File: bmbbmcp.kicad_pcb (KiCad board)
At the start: 2 copper layers, 57 x 14 mm, 20 parts, among them J1 USB_OTG, J2 Conn_ARM_SWD_TagConnect_TC2030, J3 Conn_01x04_Socket, U1 MDBT50Q-1MV2, U2 AP2112K-3.3, Y1 32.768

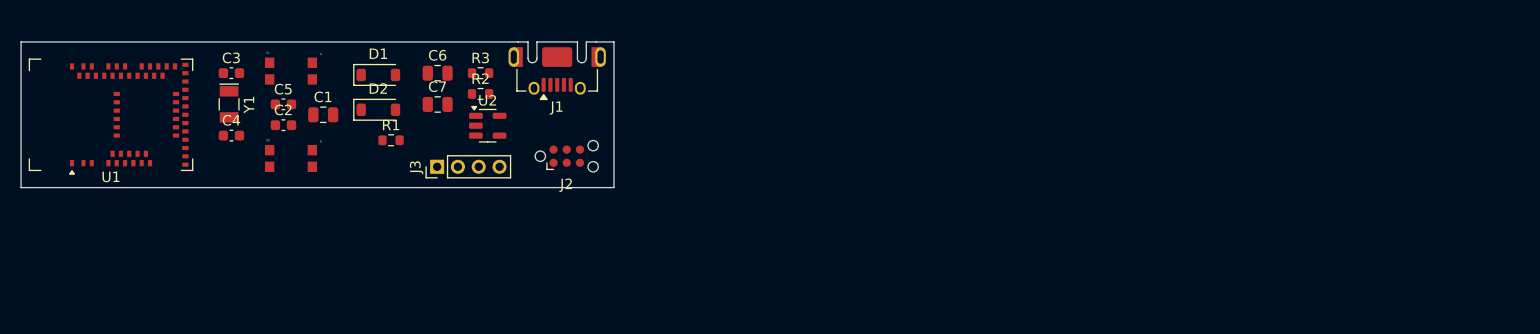
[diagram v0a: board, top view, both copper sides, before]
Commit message: Updated with routing, passes almost all design rule checks
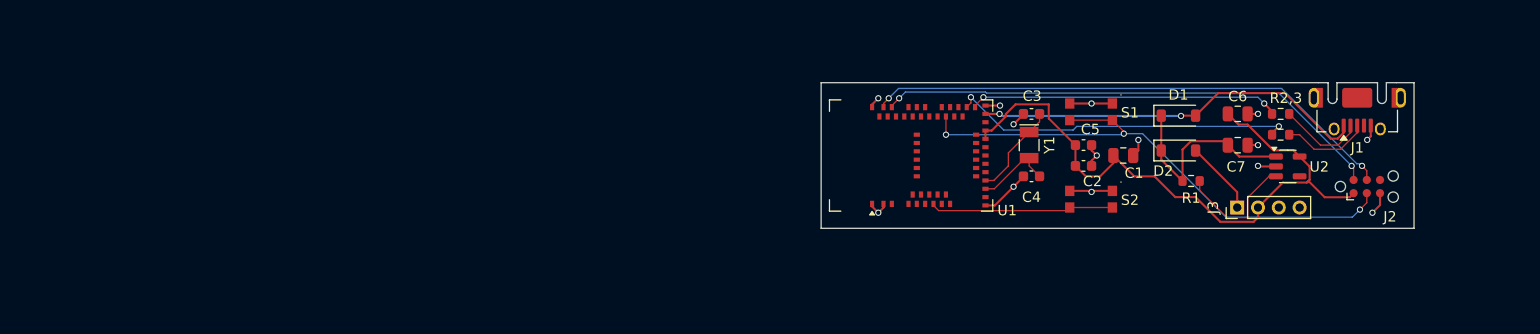
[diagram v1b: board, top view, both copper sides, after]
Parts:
- J2: value Conn_ARM_SWD_TagConnect_TC2030 -> ARM_SWD
- U2: value AP2112K-3.3 -> AP2112K
- moved R1 77.0 mm to (155.5, 95.4)
- moved C1 77.0 mm to (149.0, 92.9)
- moved C6 77.0 mm to (160.0, 88.9)
- moved C7 77.0 mm to (160.0, 91.9)
- moved J1 77.0 mm to (171.5, 87.0)
- moved R2 77.0 mm to (164.1, 90.9)
- moved R2,3 77.0 mm to (164.1, 88.9)
- moved S1 77.0 mm to (145.9, 88.7)
- moved S2 77.0 mm to (145.9, 97.1)
- moved U2 77.0 mm to (164.8, 94.0)
- moved C2 77.0 mm to (145.1, 93.9)
- moved C3 77.0 mm to (140.1, 88.9)
- moved C4 77.0 mm to (140.1, 94.9)
- moved C5 77.0 mm to (145.1, 91.9)
- moved D1 77.0 mm to (154.3, 89.1)
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- renumbered R3 to R2,3
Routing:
- net +3.3V: track 0.00 -> 60.6 mm
- net /~{RESET}: track 0.00 -> 52.9 mm, vias 0 -> 3
- net /SWCLK: track 0.00 -> 51.8 mm, vias 0 -> 2
- net /SWDIO: track 0.00 -> 49.3 mm, vias 0 -> 2
- net VBUS: track 0.00 -> 38.2 mm, vias 0 -> 2
- net /USBD+: track 0.00 -> 33.2 mm, vias 0 -> 2
- net GND: track 0.00 -> 30.7 mm, vias 0 -> 14
- net /USBD-: track 0.00 -> 29.8 mm, vias 0 -> 2
- net /VHI: track 0.00 -> 20.1 mm
- net /SWITCH: track 0.00 -> 17.7 mm
- net Net-(U2-EN): track 0.00 -> 12.1 mm
- net Net-(U1-P0.01): track 0.00 -> 9.02 mm
- net Net-(J1-D+): track 0.00 -> 8.46 mm
- net Net-(J1-D-): track 0.00 -> 8.30 mm
- net Net-(U1-P0.00): track 0.00 -> 7.59 mm
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- added copper zone on In2.Cu, net GND
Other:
- copper layers 2 -> 4

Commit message: Initial full board design
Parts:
- added C10: 10uF, Capacitor_SMD:C_0805_2012Metric, F.Cu at (160.6, 96.8)
- added C11: 0.1uF, Capacitor_SMD:C_0603_1608Metric, F.Cu at (160.6, 99.4)
- added C8: 220pF, Capacitor_SMD:C_0805_2012Metric, F.Cu at (166.4, 97.8)
- added C9: 220pF, Capacitor_SMD:C_0805_2012Metric, F.Cu at (166.4, 100.8)
- added FB1: FerriteBead, Inductor_SMD:L_0805_2012Metric, F.Cu at (162.8, 91.0)
- added FB2: FerriteBead, Inductor_SMD:L_0805_2012Metric, F.Cu at (162.9, 93.0)
- added J4: Micro_SD_Card, Connector_Card:microSD_HC_Molex_104031-0811, F.Cu at (179.9, 93.5)
- added J5: Screw_Terminal_01x02, TerminalBlock_MetzConnect:TerminalBlock_MetzConnect_Type059_RT06302HBWC_1x02_P3.50mm_Horizontal, F.Cu at (166.3, 84.0)
- added J6: Screw_Terminal_01x02, TerminalBlock_MetzConnect:TerminalBlock_MetzConnect_Type059_RT06302HBWC_1x02_P3.50mm_Horizontal, F.Cu at (155.9, 84.0)
- added J7: Screw_Terminal_01x02, TerminalBlock_MetzConnect:TerminalBlock_MetzConnect_Type059_RT06302HBWC_1x02_P3.50mm_Horizontal, F.Cu at (147.5, 84.0)
- added JP1: SolderJumper, Jumper:SolderJumper-2_P1.3mm_Bridged_RoundedPad1.0x1.5mm, F.Cu at (170.2, 89.8)
- added U3: MAX98357A, Package_DFN_QFN:TQFN-16-1EP_3x3mm_P0.5mm_EP1.23x1.23mm, F.Cu at (167.8, 94.0)
- added U4: DRV8835DSSR, DRV8835:DSS0012A, F.Cu at (156.6, 97.8)
- J2: value ARM_SWD -> Conn_ARM_SWD_TagConnect_TC2030
- J3: value Conn_01x04_Socket -> Conn_01x12_Socket; footprint Connector_PinHeader_2.00mm:PinHeader_1x04_P2.00mm_Vertical -> Connector_PinHeader_2.54mm:PinHeader_1x12_P2.54mm_Vertical
- U2: value AP2112K -> AP2112K-3.3
- moved J1 50.7 mm to (124.8, 106.9), turned to 0 degrees
- moved J2 48.9 mm to (125.1, 83.2), turned to 180 degrees
- moved R2 39.5 mm to (125.7, 100.4), turned to -90 degrees
- moved R3 38.5 mm to (127.3, 100.4), turned to -90 degrees
- moved J3 17.5 mm to (143.9, 105.0)
- moved S2 15.3 mm to (140.0, 83.0)
- moved S1 15.2 mm to (131.8, 83.0)
- moved U2 14.2 mm to (151.5, 98.9)
- moved C3 12.3 mm to (139.0, 101.2), turned to 90 degrees
- moved R1 10.8 mm to (145.1, 98.4)
- moved Y1 10.4 mm to (135.8, 101.4), turned to 180 degrees
- moved C1 10.2 mm to (139.1, 90.6)
- moved C4 9.97 mm to (132.4, 101.2), turned to 90 degrees
- moved C7 9.34 mm to (151.2, 95.0)
- moved C6 9.34 mm to (151.2, 92.0)
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- renumbered R2,3 to R3
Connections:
- J3 pad 3: unconnected-(J3-Pin_3-Pad3) -> /BTN1
- U1 pad 11: unconnected-(U1-P0.02-Pad11) -> /MOTOR_B2
- U1 pad 12: unconnected-(U1-P0.31-Pad12) -> /MOTOR_B1
- U1 pad 13: unconnected-(U1-P0.28-Pad13) -> /MOTOR_A2
- U1 pad 14: unconnected-(U1-P0.30-Pad14) -> /MOTOR_A1
- U1 pad 19: unconnected-(U1-P0.26-Pad19) -> /I2S_MODE
- U1 pad 20: unconnected-(U1-P0.04-Pad20) -> /BTN1
- U1 pad 21: unconnected-(U1-P0.05-Pad21) -> /I2S_DOUT
- U1 pad 23: unconnected-(U1-P0.07-Pad23) -> /I2S_LRCK
- U1 pad 25: unconnected-(U1-P1.08-Pad25) -> /I2S_SCK
- U1 pad 37: unconnected-(U1-P0.13-Pad37) -> /SPI_SCLK
- U1 pad 39: unconnected-(U1-P0.15-Pad39) -> /SPI_MOSI
- U1 pad 44: unconnected-(U1-P0.20-Pad44) -> /SPI_MISO
- U1 pad 50: unconnected-(U1-P1.02-Pad50) -> /SPI_CS1
- U1 pad 61: unconnected-(U1-P1.01-Pad61) -> /MOTOR_CTRL
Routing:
- net /SPI_CS1: track 0.00 -> 66.1 mm, vias 0 -> 2
- net /SPI_MISO: track 0.00 -> 61.6 mm, vias 0 -> 2
- net /SPI_MOSI: track 0.00 -> 59.0 mm, vias 0 -> 2
- net /SPI_SCLK: track 0.00 -> 58.9 mm, vias 0 -> 2
- net +3.3V: track 60.6 -> 115.7 mm, vias 0 -> 6
- net /SWCLK: track 51.8 -> 4.72 mm, vias 2 -> 0
- net /I2S_MODE: track 0.00 -> 45.9 mm, vias 0 -> 2
- net /SWDIO: track 49.3 -> 4.53 mm, vias 2 -> 0
- net /I2S_DOUT: track 0.00 -> 43.7 mm, vias 0 -> 2
- net /I2S_LRCK: track 0.00 -> 41.6 mm, vias 0 -> 2
- net /I2S_SCK: track 0.00 -> 40.4 mm, vias 0 -> 2
- net /MOTOR_CTRL: track 0.00 -> 36.6 mm, vias 0 -> 2
- net /~{RESET}: track 52.9 -> 16.4 mm, vias 3 -> 0
- net /MOTOR_B1: track 0.00 -> 35.7 mm, vias 0 -> 2
- net /MOTOR_B2: track 0.00 -> 30.8 mm, vias 0 -> 2
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- added copper zone on In1.Cu, net GND
- removed copper zone on In2.Cu, net GND
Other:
- board size 57 x 14 mm -> 68 x 28 mm

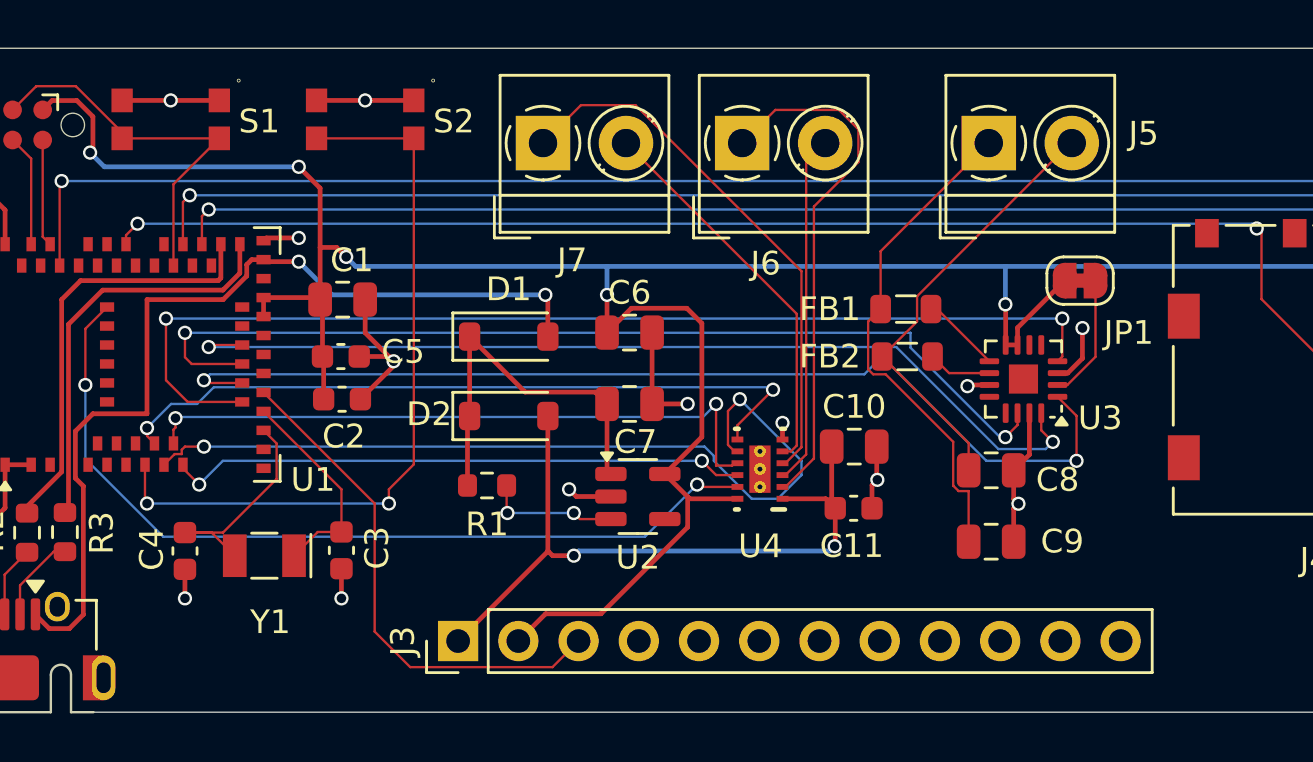
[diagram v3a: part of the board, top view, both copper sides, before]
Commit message: Switch to three pin
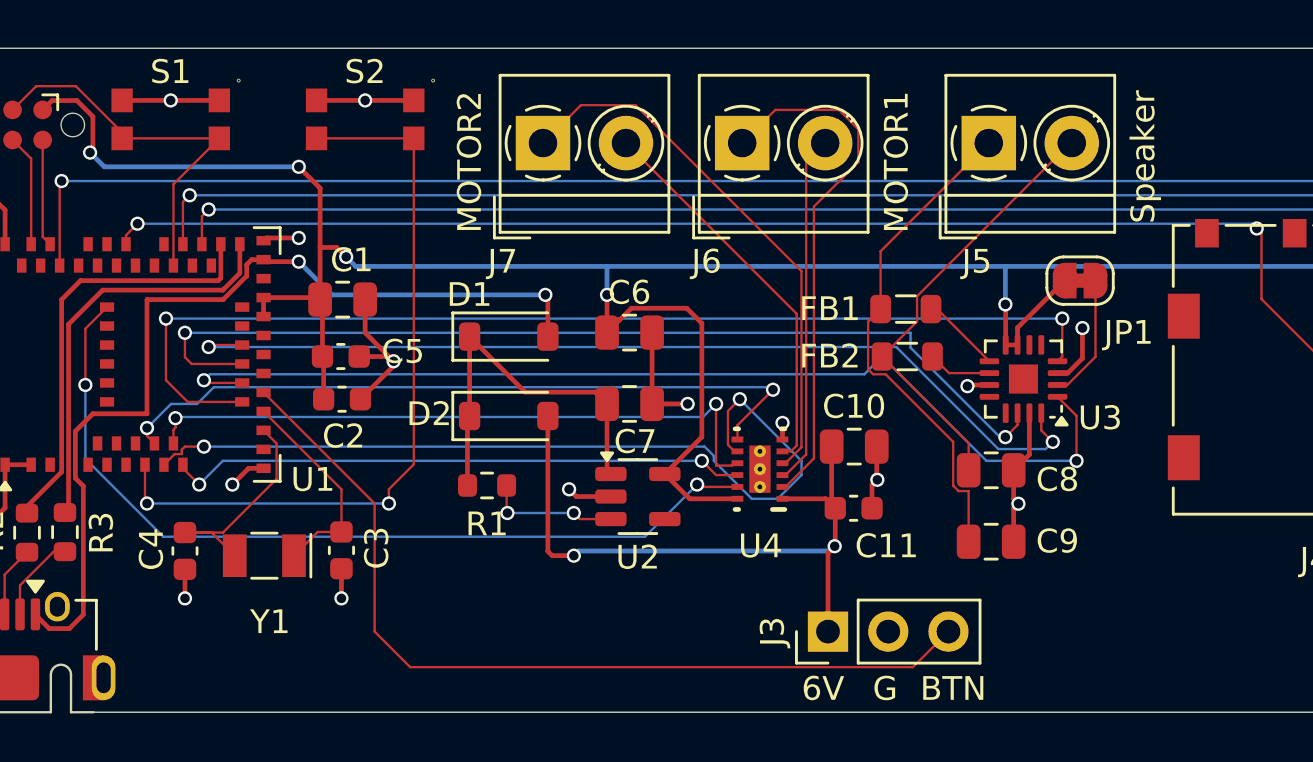
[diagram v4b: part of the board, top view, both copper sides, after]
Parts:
- added REF**: OSHW-Logo_5.7x6mm_SilkScreen, Symbol:OSHW-Logo_5.7x6mm_SilkScreen, B.Cu at (123.6, 93.6)
- added REF**: KiCad-Logo2_6mm_SilkScreen, Symbol:KiCad-Logo2_6mm_SilkScreen, B.Cu at (176.0, 102.3)
- J3: value Conn_01x12_Socket -> Conn_01x03_Pin; footprint Connector_PinHeader_2.54mm:PinHeader_1x12_P2.54mm_Vertical -> Connector_PinHeader_2.54mm:PinHeader_1x03_P2.54mm_Vertical
- moved J3 15.6 mm to (159.5, 104.6)
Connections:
- J3 pad 2: +3.3V -> GND
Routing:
- net /BTN1: track 21.7 -> 37.5 mm
- net +3.3V: track 115.7 -> 105.3 mm
- net +BATT: track 30.1 -> 28.4 mm
- net GND: track 55.4 -> 56.9 mm, vias 17 -> 18
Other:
- board text added: "6V"
- board text added: "BTN"
- board text added: "G"
- board text added: "MOTOR1"
- board text added: "MOTOR2"
- board text added: "Speaker"
- board text added: "Tasty Cactus BMBB R1"

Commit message: Switch MCU from MDBT50Q-1MV2 to MDBT50Q-P1MV2 (PCB antenna version, in stock)
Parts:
- U1: value MDBT50Q-1MV2 -> MDBT50Q-P1MV2
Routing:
- net GND: track 56.9 -> 56.2 mm
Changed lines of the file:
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@@
 		(sheetname "components")
 		(sheetfile "components.kicad_sch")
-		(attr through_hole exclude_from_pos_files exclude_from_bom)
+		(attr through_hole exclude_from_pos_files)
 		(fp_line
 			(start -2.05 2.26)
@@
 		(sheetname "components")
 		(sheetfile "components.kicad_sch")
-		(attr through_hole exclude_from_pos_files exclude_from_bom)
+		(attr through_hole exclude_from_pos_files)
 		(fp_line
 			(start -2.05 2.26)
@@
 		(sheetname "Root")
 		(sheetfile "bmbbmcp.kicad_sch")
-		(attr through_hole exclude_from_pos_files exclude_from_bom)
+		(attr through_hole exclude_from_pos_files)
 		(fp_line
 			(start -1.33 -1.33)
@@
 		)
 		(fp_text user "${REFERENCE}"
-			(at 0 2.54 360)
+			(at 0 2.54 0)
 			(layer "F.Fab")
 			(effects
@@
 			)
 		)
-		(property "Value" "MDBT50Q-1MV2"
+		(property "Value" "MDBT50Q-P1MV2"
 			(at -3 -0.05 180)
 			(layer "F.Fab")
@@
 		(sheetname "components")
 		(sheetfile "components.kicad_sch")
-		(attr through_hole exclude_from_pos_files exclude_from_bom)
+		(attr through_hole exclude_from_pos_files)
 		(fp_line
 			(start -2.05 2.26)
@@
 		(width 0.2)
 		(layer "F.Cu")
-		(net 2)
-	)
-	(segment
-		(start 156.650002 96.999999)
-		(end 156.650002 97.749997)
-		(width 0.2)
-		(layer "F.Cu")
